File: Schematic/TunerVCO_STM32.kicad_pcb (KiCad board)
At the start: 4 copper layers, 45.7 x 110 mm, 82 parts, among them J101 1V/OCT, J102 FM, J103 HARD SYNC, J104 SOFT SYNC, J105 PWM, J106 Pulse, J107 Saw, J108 Triangle, J109 POWER, J110 SWI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

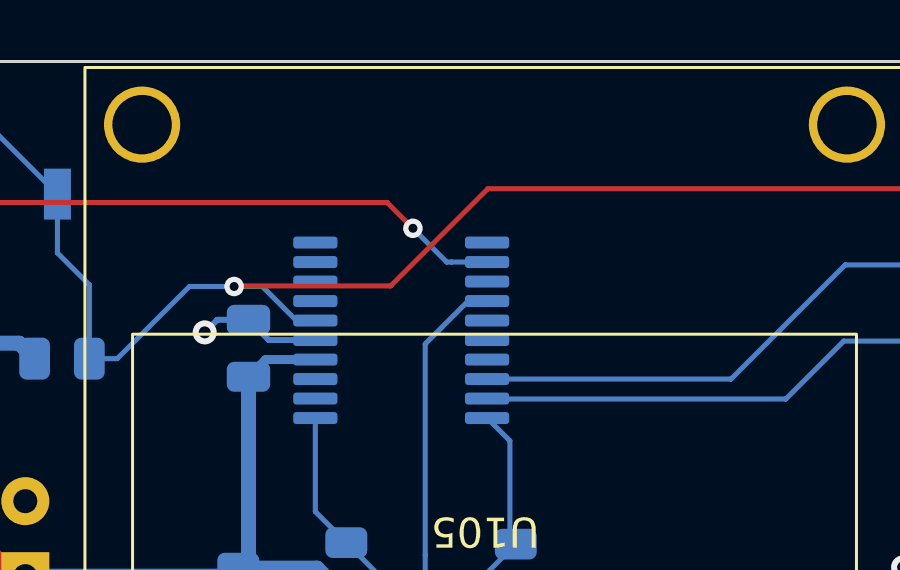
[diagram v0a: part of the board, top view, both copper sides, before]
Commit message: main while loop, fixed pinout
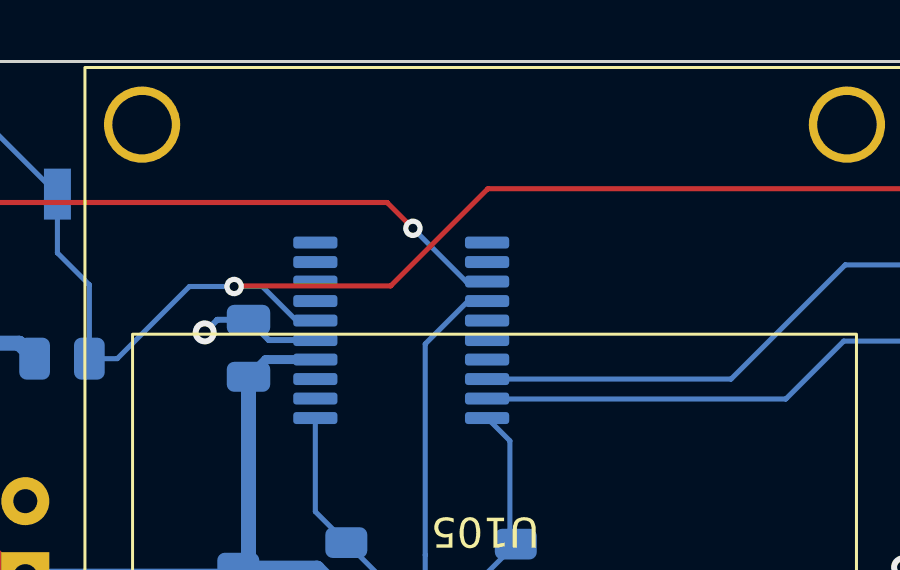
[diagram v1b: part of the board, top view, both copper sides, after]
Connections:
- U104 pad 12: PIXEL -> unconnected-(U104-PA5-Pad12)
- U104 pad 13: unconnected-(U104-PA6-Pad13) -> PIXEL
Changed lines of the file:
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@@
   (net 70 "unconnected-(U104-PA3-Pad10)")
   (net 71 "unconnected-(U104-PA4-Pad11)")
-  (net 72 "unconnected-(U104-PA6-Pad13)")
+  (net 72 "unconnected-(U104-PA5-Pad12)")
   (net 73 "unconnected-(U104-PB0{slash}PB1{slash}PB2{slash}PA8-Pad15)")
   (net 74 "unconnected-(U104-PA11{slash}PA9-Pad16)")
@@
       (net 71 "unconnected-(U104-PA4-Pad11)") (pinfunction "PA4") (pintype "bidirectional+no_connect"))
     (pad "12" smd roundrect (at 2.8625 -2.275) (size 1.475 0.4) (layers "B.Cu" "B.Paste" "B.Mask") (roundrect_rratio 0.25)
-      (net 61 "PIXEL") (pinfunction "PA5") (pintype "bidirectional"))
+      (net 72 "unconnected-(U104-PA5-Pad12)") (pinfunction "PA5") (pintype "bidirectional+no_connect"))
     (pad "13" smd roundrect (at 2.8625 -1.625) (size 1.475 0.4) (layers "B.Cu" "B.Paste" "B.Mask") (roundrect_rratio 0.25)
-      (net 72 "unconnected-(U104-PA6-Pad13)") (pinfunction "PA6") (pintype "bidirectional+no_connect"))
+      (net 61 "PIXEL") (pinfunction "PA6") (pintype "bidirectional"))
     (pad "14" smd roundrect (at 2.8625 -0.975) (size 1.475 0.4) (layers "B.Cu" "B.Paste" "B.Mask") (roundrect_rratio 0.25)
       (net 26 "V_INTR") (pinfunction "PA7") (pintype "bidirectional"))
@@
   (segment (start 1.91 10.78) (end 3.06 11.93) (width 0.17) (layer "F.Cu") (net 61))
   (via (at 22.56 5.56) (size 0.65) (drill 0.3) (layers "F.Cu" "B.Cu") (net 61))
-  (segment (start 25.0325 6.685) (end 23.845 6.685) (width 0.17) (layer "B.Cu") (net 61))
-  (segment (start 23.685 6.685) (end 22.56 5.56) (width 0.17) (layer "B.Cu") (net 61))
-  (segment (start 23.845 6.685) (end 23.685 6.685) (width 0.17) (layer "B.Cu") (net 61))
+  (segment (start 25.0325 7.335) (end 24.335 7.335) (width 0.17) (layer "B.Cu") (net 61))
+  (segment (start 24.335 7.335) (end 22.56 5.56) (width 0.17) (layer "B.Cu") (net 61))
   (segment (start 25.0475 11.25) (end 25.0325 11.235) (width 0.17) (layer "B.Cu") (net 62))
   (segment (start 34.99 11.25) (end 25.0475 11.25) (width 0.17) (layer "B.Cu") (net 62))
